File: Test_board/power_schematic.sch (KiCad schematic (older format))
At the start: 65 parts, among them J10 4.19mmBananaJack, J9 4.19mmBananaJack, U3 LT3652, U5 LT3652, U7 LM193, U8 TPS22965-Q1, U9 TPS22965-Q1

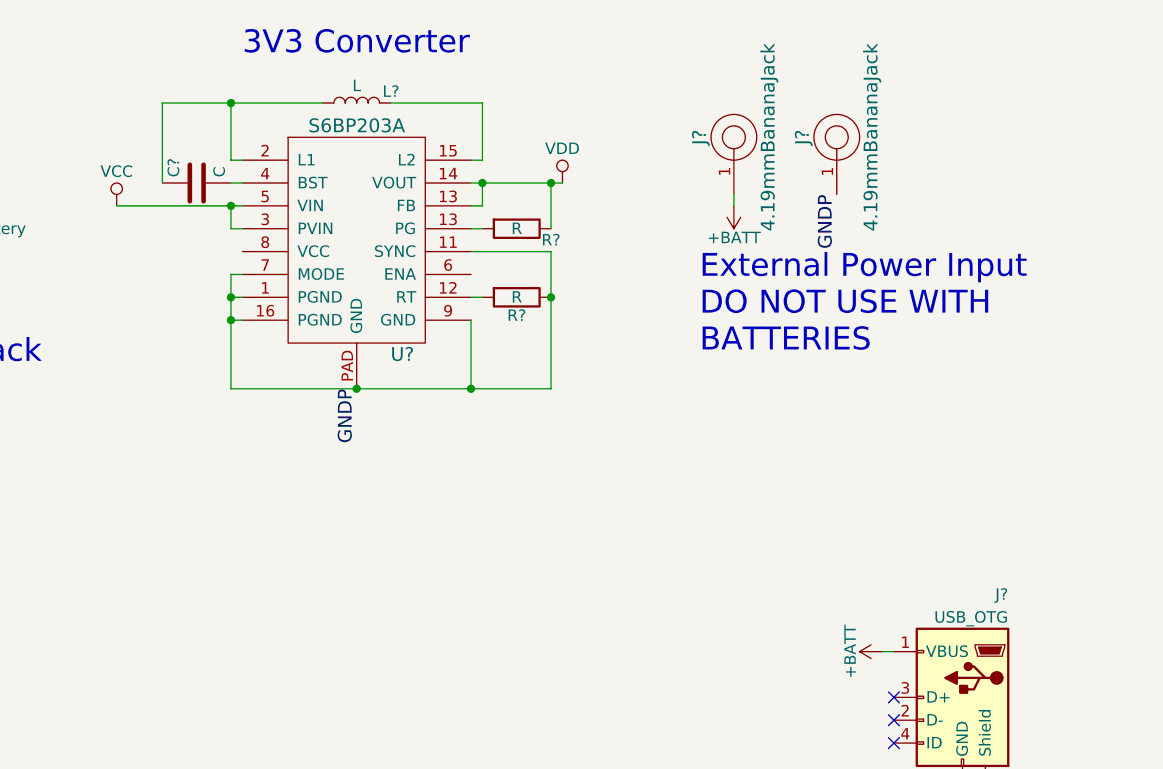
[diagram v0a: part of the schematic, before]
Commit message: Added programming header to diagram. Changed drafting template
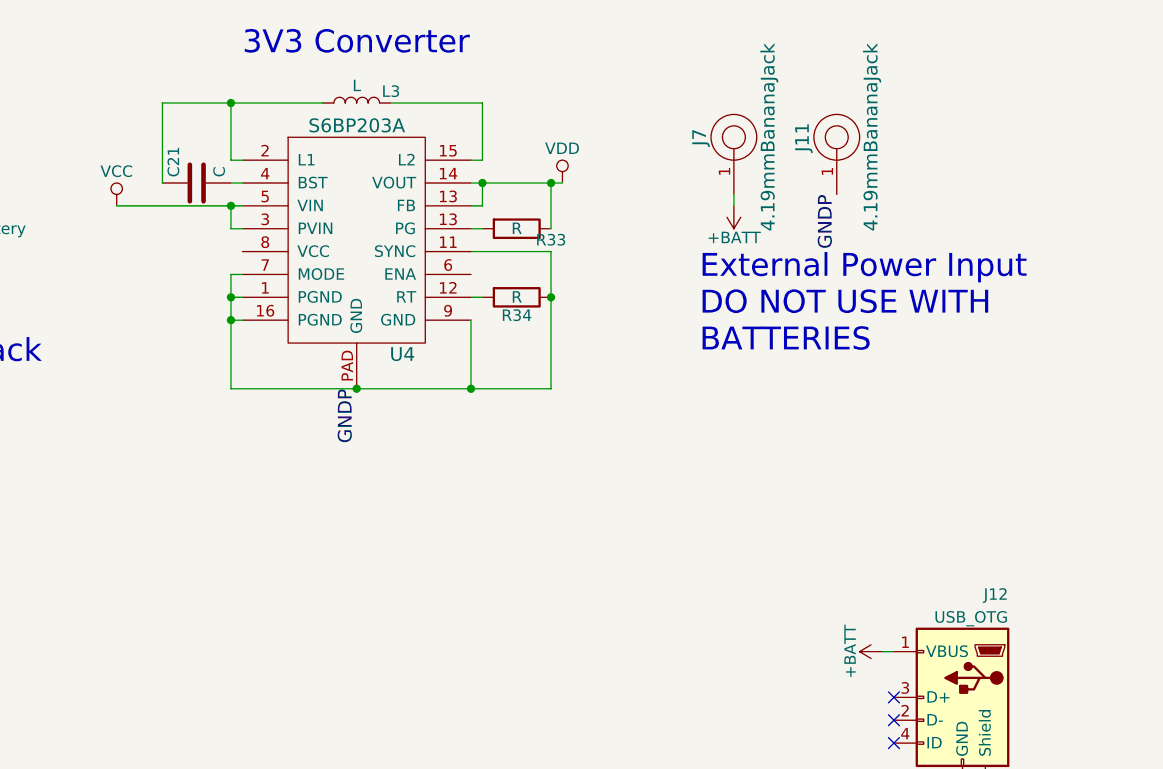
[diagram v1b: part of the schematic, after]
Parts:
- gave numbers to parts that had none: 8
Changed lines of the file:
@@
 $EndComp
 $Comp
-L +BATT #PWR045
+L +BATT #PWR034
 U 1 1 59AC4DF1
 P 5150 1100
-F 0 "#PWR045" H 5150 950 50  0001 C CNN
+F 0 "#PWR034" H 5150 950 50  0001 C CNN
 F 1 "+BATT" H 5150 1240 50  0000 C CNN
 F 2 "" H 5150 1100 50  0001 C CNN
@@
 $EndComp
 $Comp
-L +BATT #PWR046
+L +BATT #PWR035
 U 1 1 59AC5ACD
 P 5200 3050
-F 0 "#PWR046" H 5200 2900 50  0001 C CNN
+F 0 "#PWR035" H 5200 2900 50  0001 C CNN
 F 1 "+BATT" H 5200 3190 50  0000 C CNN
 F 2 "" H 5200 3050 50  0001 C CNN
@@
 $EndComp
 $Comp
-L VCC #PWR047
+L VCC #PWR036
 U 1 1 59AC8C79
 P 7000 1250
-F 0 "#PWR047" H 7000 1100 50  0001 C CNN
+F 0 "#PWR036" H 7000 1100 50  0001 C CNN
 F 1 "VCC" H 7000 1400 50  0000 C CNN
 F 2 "" H 7000 1250 50  0001 C CNN
@@
 $EndComp
 $Comp
-L +BATT #PWR048
+L +BATT #PWR037
 U 1 1 59AC8F41
 P 6250 1100
-F 0 "#PWR048" H 6250 950 50  0001 C CNN
+F 0 "#PWR037" H 6250 950 50  0001 C CNN
 F 1 "+BATT" H 6250 1240 50  0000 C CNN
 F 2 "" H 6250 1100 50  0001 C CNN
@@
 GNDP
 $Comp
-L VDD #PWR049
+L VDD #PWR038
 U 1 1 59AC5266
 P 8950 1150
-F 0 "#PWR049" H 8950 1000 50  0001 C CNN
+F 0 "#PWR038" H 8950 1000 50  0001 C CNN
 F 1 "VDD" H 8950 1300 50  0000 C CNN
 F 2 "" H 8950 1150 50  0001 C CNN
@@
 GNDP
 $Comp
-L +BATT #PWR050
+L +BATT #PWR039
 U 1 1 59ADB277
 P 9700 1250
-F 0 "#PWR050" H 9700 1100 50  0001 C CNN
+F 0 "#PWR039" H 9700 1100 50  0001 C CNN
 F 1 "+BATT" H 9700 1390 50  0000 C CNN
 F 2 "" H 9700 1250 50  0001 C CNN
@@
 $EndComp
 $Comp
-L +3V3 #PWR051
+L +3V3 #PWR040
 U 1 1 59ADC4C6
 P 1250 4800
-F 0 "#PWR051" H 1250 4650 50  0001 C CNN
+F 0 "#PWR040" H 1250 4650 50  0001 C CNN
 F 1 "+3V3" H 1250 4940 50  0000 C CNN
 F 2 "" H 1250 4800 50  0001 C CNN
@@
 $EndComp
 $Comp
-L GND #PWR052
+L GND #PWR041
 U 1 1 59ADF186
 P 1250 5800
-F 0 "#PWR052" H 1250 5550 50  0001 C CNN
+F 0 "#PWR041" H 1250 5550 50  0001 C CNN
 F 1 "GND" H 1250 5650 50  0000 C CNN
 F 2 "" H 1250 5800 50  0001 C CNN
@@
 $EndComp
 $Comp
-L +3V3 #PWR053
+L +3V3 #PWR042
 U 1 1 59AE06AA
 P 1250 6450
-F 0 "#PWR053" H 1250 6300 50  0001 C CNN
+F 0 "#PWR042" H 1250 6300 50  0001 C CNN
 F 1 "+3V3" H 1250 6590 50  0000 C CNN
 F 2 "" H 1250 6450 50  0001 C CNN
@@
 $EndComp
 $Comp
-L GND #PWR054
+L GND #PWR043
 U 1 1 59AE06CE
 P 1250 7450
-F 0 "#PWR054" H 1250 7200 50  0001 C CNN
+F 0 "#PWR043" H 1250 7200 50  0001 C CNN
 F 1 "GND" H 1250 7300 50  0000 C CNN
 F 2 "" H 1250 7450 50  0001 C CNN
@@
 $EndComp
 $Comp
-L +3V3 #PWR055
+L +3V3 #PWR044
 U 1 1 59AE405D
 P 2850 4900
-F 0 "#PWR055" H 2850 4750 50  0001 C CNN
+F 0 "#PWR044" H 2850 4750 50  0001 C CNN
 F 1 "+3V3" H 2850 5040 50  0000 C CNN
 F 2 "" H 2850 4900 50  0001 C CNN
@@
 Battery Heaters
 $Comp
-L +BATT #PWR056
+L +BATT #PWR045
 U 1 1 59AEABD5
 P 3150 5050
-F 0 "#PWR056" H 3150 4900 50  0001 C CNN
+F 0 "#PWR045" H 3150 4900 50  0001 C CNN
 F 1 "+BATT" H 3150 5190 50  0000 C CNN
 F 2 "" H 3150 5050 50  0001 C CNN
@@
 $EndComp
 $Comp
-L +BATT #PWR057
+L +BATT #PWR046
 U 1 1 59AEAD99
 P 3200 6700
-F 0 "#PWR057" H 3200 6550 50  0001 C CNN
+F 0 "#PWR046" H 3200 6550 50  0001 C CNN
 F 1 "+BATT" H 3200 6840 50  0000 C CNN
 F 2 "" H 3200 6700 50  0001 C CNN
@@
 $EndComp
 $Comp
-L GND #PWR058
+L GND #PWR047
 U 1 1 59AEECE6
 P 1250 1300
-F 0 "#PWR058" H 1250 1050 50  0001 C CNN
+F 0 "#PWR047" H 1250 1050 50  0001 C CNN
 F 1 "GND" H 1250 1150 50  0000 C CNN
 F 2 "" H 1250 1300 50  0001 C CNN
@@
 $EndComp
 $Comp
-L +3V3 #PWR059
+L +3V3 #PWR048
 U 1 1 59AF8E23
 P 2550 6550
-F 0 "#PWR059" H 2550 6400 50  0001 C CNN
+F 0 "#PWR048" H 2550 6400 50  0001 C CNN
 F 1 "+3V3" H 2550 6690 50  0000 C CNN
 F 2 "" H 2550 6550 50  0001 C CNN
@@
 GNDP
 $Comp
-L USB_OTG J?
+L USB_OTG J12
 U 1 1 59DBF217
 P 10700 3400
-F 0 "J?" H 10500 3850 50  0000 L CNN
+F 0 "J12" H 10500 3850 50  0000 L CNN
 F 1 "USB_OTG" H 10500 3750 50  0000 L CNN
 F 2 "" H 10850 3350 50  0001 C CNN
@@
 NoConn ~ 10400 3500
 $Comp
-L +BATT #PWR?
+L +BATT #PWR049
 U 1 1 59DBF4CB
 P 10350 3200
-F 0 "#PWR?" H 10350 3050 50  0001 C CNN
+F 0 "#PWR049" H 10350 3050 50  0001 C CNN
 F 1 "+BATT" H 10350 3340 50  0000 C CNN
 F 2 "" H 10350 3200 50  0001 C CNN
@@
 GNDP
 $Comp
-L S6BP203A U?
+L S6BP203A U4
 U 1 1 59DBFB58
 P 8050 1400
-F 0 "U?" H 8250 900 60  0000 C CNN
+F 0 "U4" H 8250 900 60  0000 C CNN
 F 1 "S6BP203A" H 8050 1900 60  0000 C CNN
 F 2 "" H 8050 1250 60  0001 C CNN
@@
 Connection ~ 7500 1250
 $Comp
-L L L?
+L L L3
 U 1 1 59DC0813
 P 8050 800
-F 0 "L?" V 8100 650 50  0000 C CNN
+F 0 "L3" V 8100 650 50  0000 C CNN
 F 1 "L" V 8125 800 50  0000 C CNN
 F 2 "" H 8050 800 50  0001 C CNN
@@
 	8600 1050 8550 1050
 $Comp
-L C C?
+L C C21
 U 1 1 59DC12D3
 P 7350 1150
-F 0 "C?" H 7375 1250 50  0000 L CNN
+F 0 "C21" H 7375 1250 50  0000 L CNN
 F 1 "C" H 7375 1050 50  0000 L CNN
 F 2 "" H 7388 1000 50  0001 C CNN
@@
 Connection ~ 8600 1150
 $Comp
-L R R?
+L R R34
 U 1 1 59DC1D9B
 P 8750 1650
-F 0 "R?" V 8830 1650 50  0000 C CNN
+F 0 "R34" V 8830 1650 50  0000 C CNN
 F 1 "R" V 8750 1650 50  0000 C CNN
 F 2 "" V 8680 1650 50  0001 C CNN
@@
 Connection ~ 8550 2050
 $Comp
-L R R?
+L R R33
 U 1 1 59DC2107
 P 8750 1350
-F 0 "R?" V 8800 1500 50  0000 C CNN
+F 0 "R33" V 8800 1500 50  0000 C CNN
 F 1 "R" V 8750 1350 50  0000 C CNN
 F 2 "" V 8680 1350 50  0001 C CNN
@@
 Connection ~ 8900 1650
 $Comp
-L 4.19mmBananaJack J?
+L 4.19mmBananaJack J7
 U 1 1 59DC400B
 P 9700 950
-F 0 "J?" H 9700 800 60  0000 C CNN
+F 0 "J7" H 9700 800 60  0000 C CNN
 F 1 "4.19mmBananaJack" H 9700 1100 60  0000 C CNN
 F 2 "" H 9700 950 60  0001 C CNN
@@
 $EndComp
 $Comp
-L 4.19mmBananaJack J?
+L 4.19mmBananaJack J11
 U 1 1 59DC40B4
 P 10150 950
-F 0 "J?" H 10150 800 60  0000 C CNN
+F 0 "J11" H 10150 800 60  0000 C CNN
 F 1 "4.19mmBananaJack" H 10150 1100 60  0000 C CNN
 F 2 "" H 10150 950 60  0001 C CNN
